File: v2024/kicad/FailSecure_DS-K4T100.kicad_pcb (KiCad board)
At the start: 4 copper layers, 95.8 x 79 mm, 82 parts, among them CN1 WJ2EDGRC-5.08-2P, CN2 WJ2EDGRC-5.08-2P, CN3 WJ2EDGRC-5.08-8P, CN4 WAFER-200W-4P, CN5 WJ2EDGRC-5.08-2P, Q1 BSS138, Q3 BSS138, Q4 BSS138, SW1 1TS002B-2300-4301, SW2 1TS002B-2300-4301, U1 PicoW, U2 TPS563200DDCR, U3 BX-DS2.54-4PTP, U4 SFH6206-3T, U5 HX PM2.54-2X5P WT, U6 HX PM2.54-2X5P WT

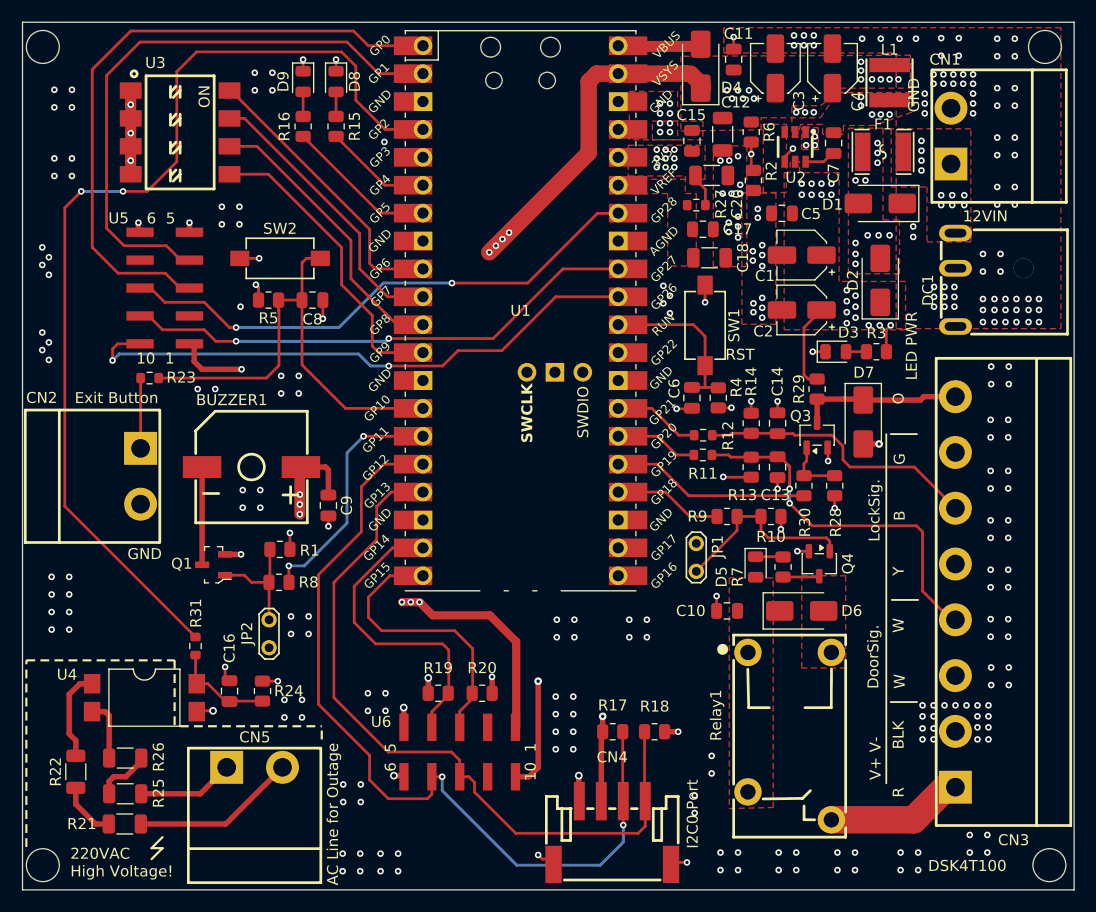
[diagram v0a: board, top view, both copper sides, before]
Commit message: Kicad, add LCSC part number to forgotten devices & Don't populate jumper
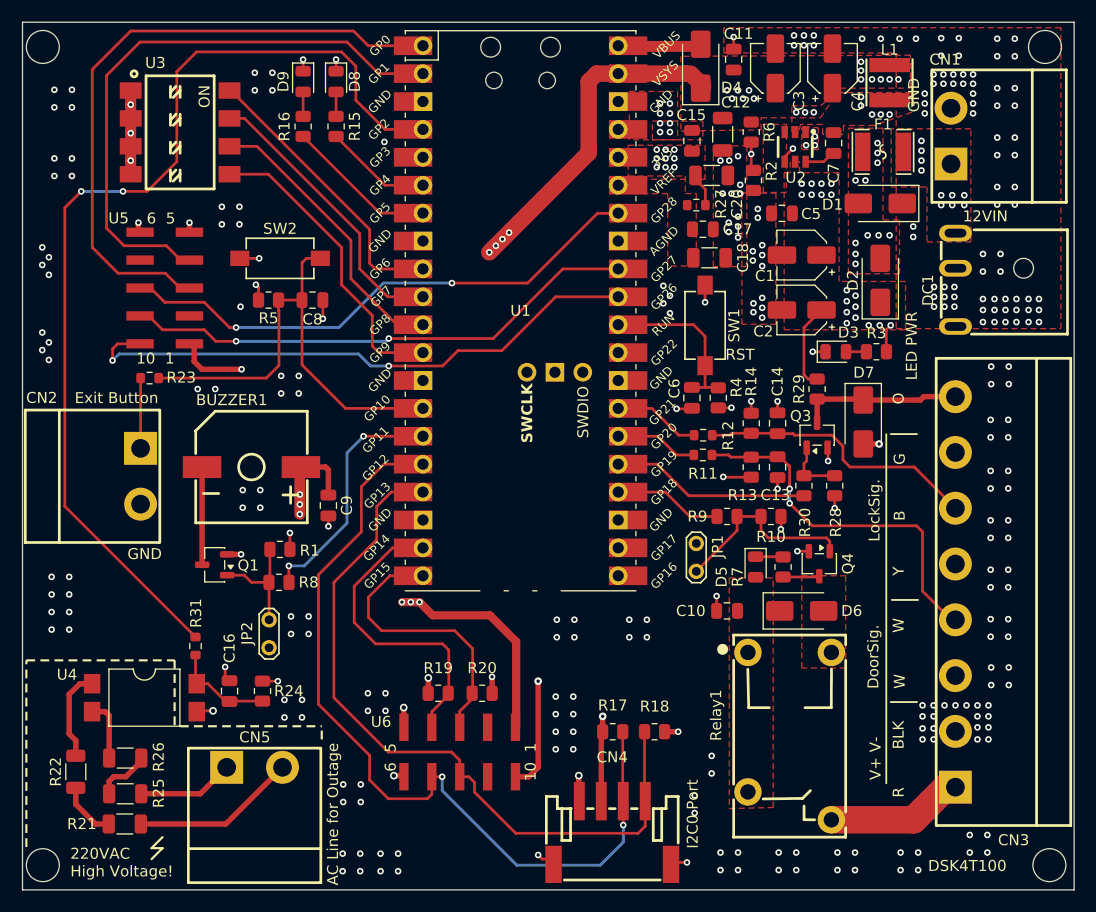
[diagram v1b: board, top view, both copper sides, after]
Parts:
- Q1: footprint digikey-footprints:SOT-23-3 -> Package_TO_SOT_SMD:SOT-23-3
- moved Q1 0.10 mm to (115.2, 114.4)

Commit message: update PCB silkscreen
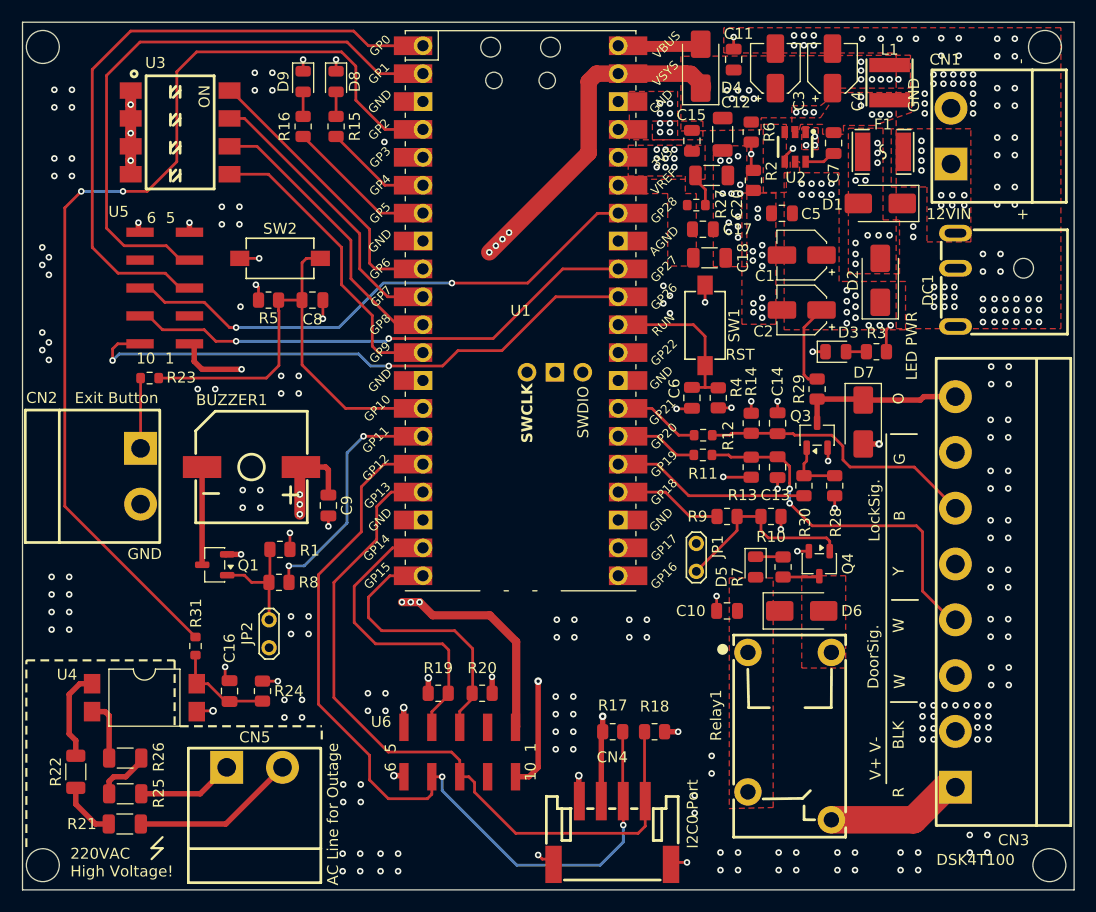
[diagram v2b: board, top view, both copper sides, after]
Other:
- board text added: "+"
- board text added: "-"
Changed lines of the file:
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@@
 		(at 110.6 89.2 90)
 		(property "Reference" "U5"
-			(at 6.35 -4.2 180)
+			(at 6.95 -4.2 180)
 			(layer "F.SilkS")
 			(effects
@@
 	)
 	(gr_text "6  5"
-		(at 108.95 83.45 0)
+		(at 108.95 83.4 0)
 		(layer "F.SilkS")
 		(effects
@@
 		)
 	)
+	(gr_text "-"
+		(at 189.1 68.8 90)
+		(layer "F.SilkS")
+		(effects
+			(font
+				(size 1 1)
+				(thickness 0.16)
+			)
+			(justify left bottom)
+		)
+	)
 	(gr_text "DSK4T100"
-		(at 180.1 142.4 0)
+		(at 180.85 141.85 0)
 		(layer "F.SilkS")
 		(effects
@@
 		)
 	)
+	(gr_text "+"
+		(at 188.15 83.05 0)
+		(layer "F.SilkS")
+		(effects
+			(font
+				(size 1 1)
+				(thickness 0.16)
+			)
+			(justify left bottom)
+		)
+	)
 	(gr_text "W"
 		(at 178 120.6 90)
@@
 	)
 	(gr_text "12VIN"
-		(at 183.25 83.25 0)
-		(layer "F.SilkS")
-		(effects
+		(at 179.95 83.05 0)
+		(layer "F.SilkS")
+		(effects

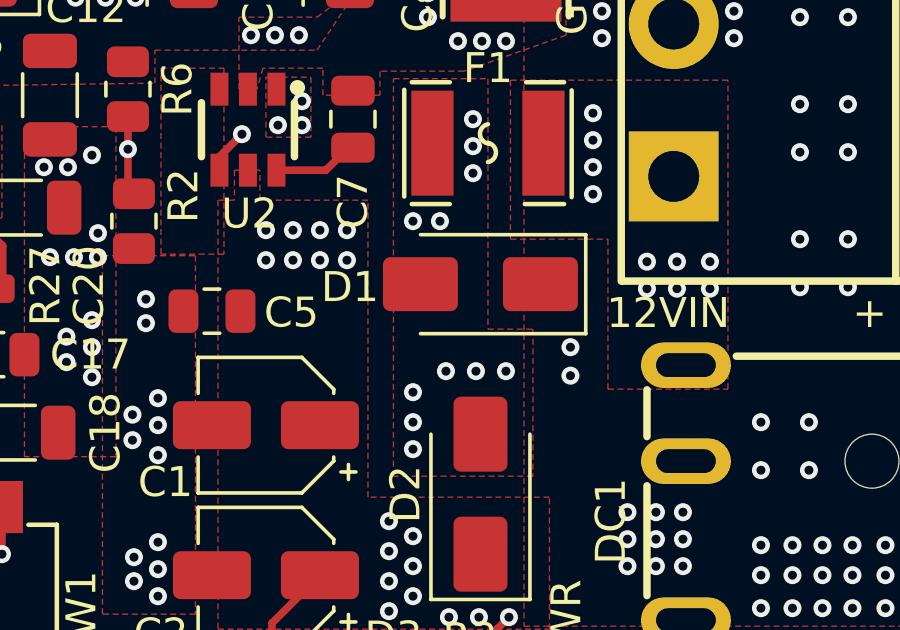
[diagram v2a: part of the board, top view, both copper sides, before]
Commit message: Update BOM by remove extended part as much as posible
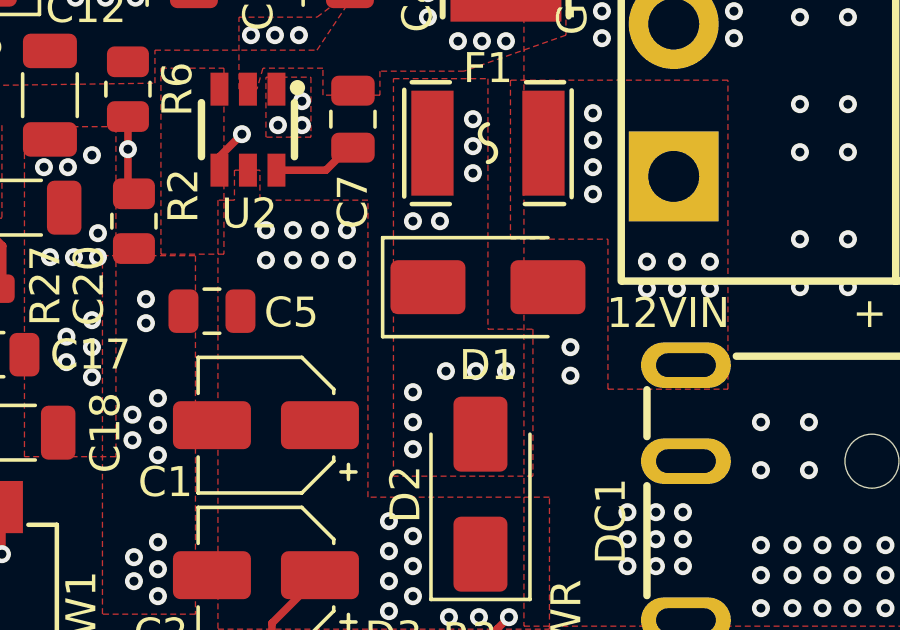
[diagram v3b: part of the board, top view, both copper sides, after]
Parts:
- D1: value SMAJ26CA -> SMAJ26A
- D5: value Red -> Yellow
- moved D1 0.27 mm to (176.0, 81.6), turned to 0 degrees
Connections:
- D1 pad 1: GND -> Net-(D1-A1)
- D1 pad 2: Net-(D1-A2) -> GND
- D2 pad 2: Net-(D1-A2) -> Net-(D1-A1)
- F1 pad 2: Net-(D1-A2) -> Net-(D1-A1)
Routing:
- net Net-(D1-A2): vias 11 -> 0
- net Net-(D1-A1): vias 0 -> 11
- added copper zone on F.Cu, net Net-(D1-A1)
- added copper zone on In2.Cu, net Net-(D1-A1)
- removed copper zone on F.Cu, net Net-(D1-A2)
- removed copper zone on In2.Cu, net Net-(D1-A2)
